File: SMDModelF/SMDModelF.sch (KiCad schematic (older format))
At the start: 45 parts, among them J1 Model F Ribbon Cable, J2 PadsToShort, J3 EXPANSION HEADER, J4 3178 Ribbon Cable, J6 MODEL F AT LOCKLIGHTS HEADER, U1 MCP4921-E, U2 LM339A, U3 74AHC595, U4 74AHC595, U5 ProMicro, U6 LM339A

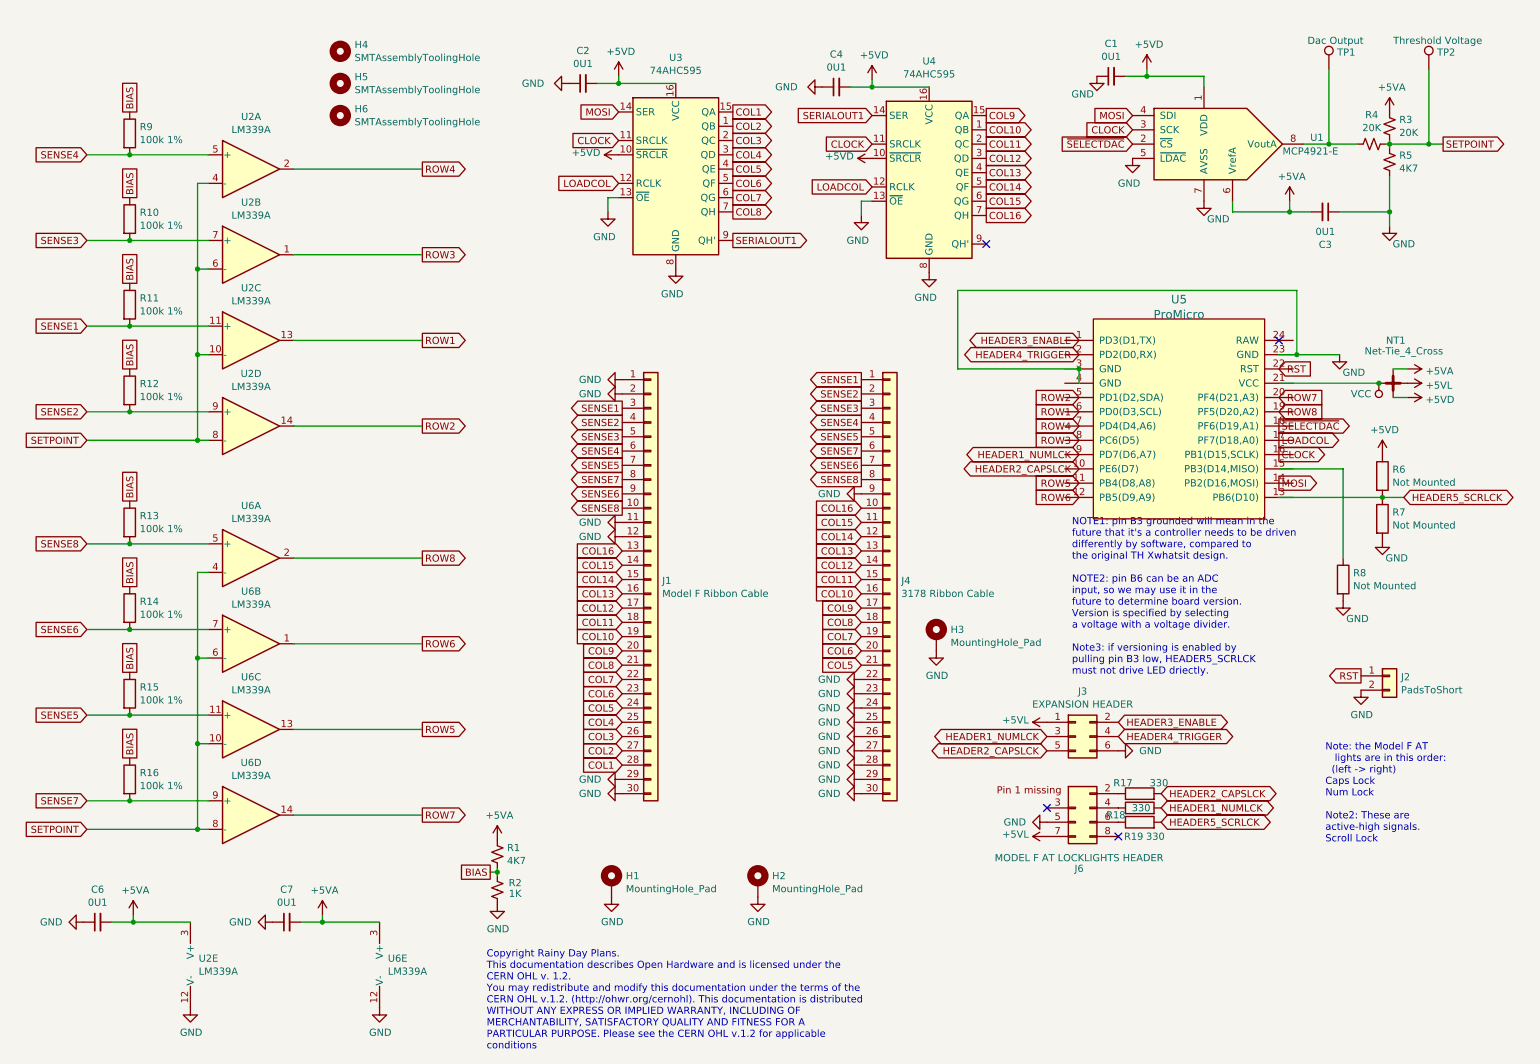
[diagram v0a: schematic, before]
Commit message: Added extra columns
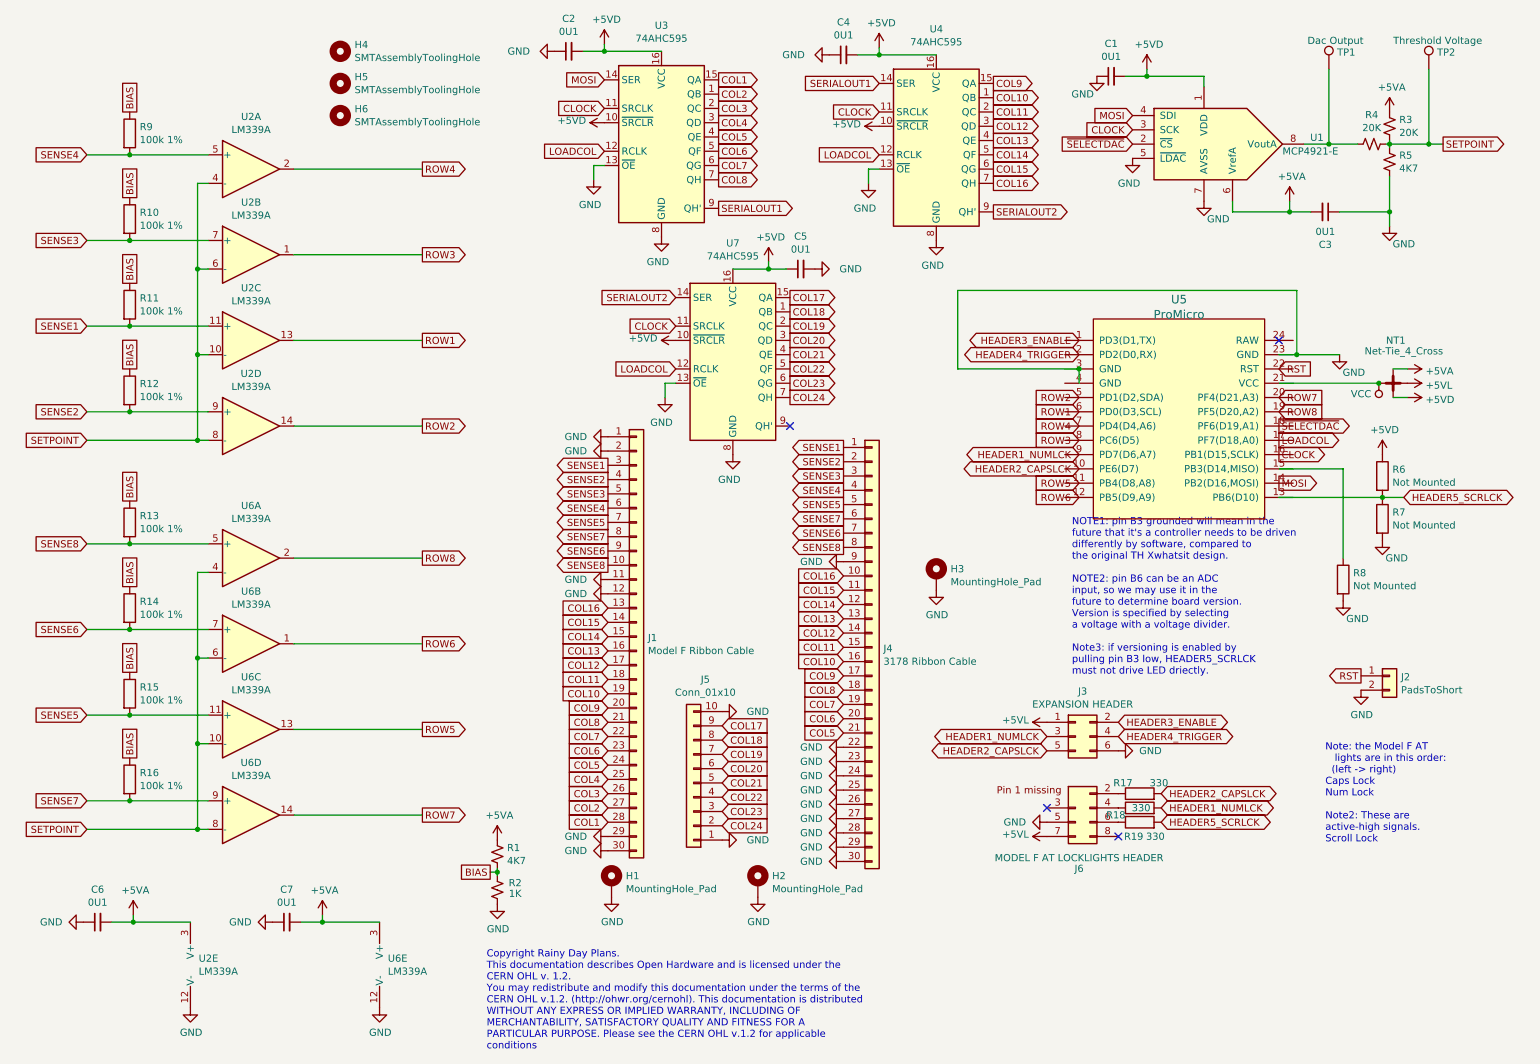
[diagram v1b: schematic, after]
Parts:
- added C5: 0U1, Capacitor_SMD:C_0805_2012Metric_Pad1.15x1.40mm_HandSolder, symbol Device:C_Small
- added J5: Conn_01x10, Connector_PinHeader_2.54mm:PinHeader_1x10_P2.54mm_Vertical, symbol Connector_Generic:Conn_01x10
- added U7: 74AHC595, Package_SO:SOIC-16_3.9x9.9mm_P1.27mm, symbol 74xx:74HCT595
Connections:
- net labels added: COL17, COL18, COL19, COL20, COL21, COL22, COL23, COL24, SERIALOUT2
- wire segments 93 -> 98
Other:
- moved on the sheet: C2, C4, H3, J1, J4, U3, U4

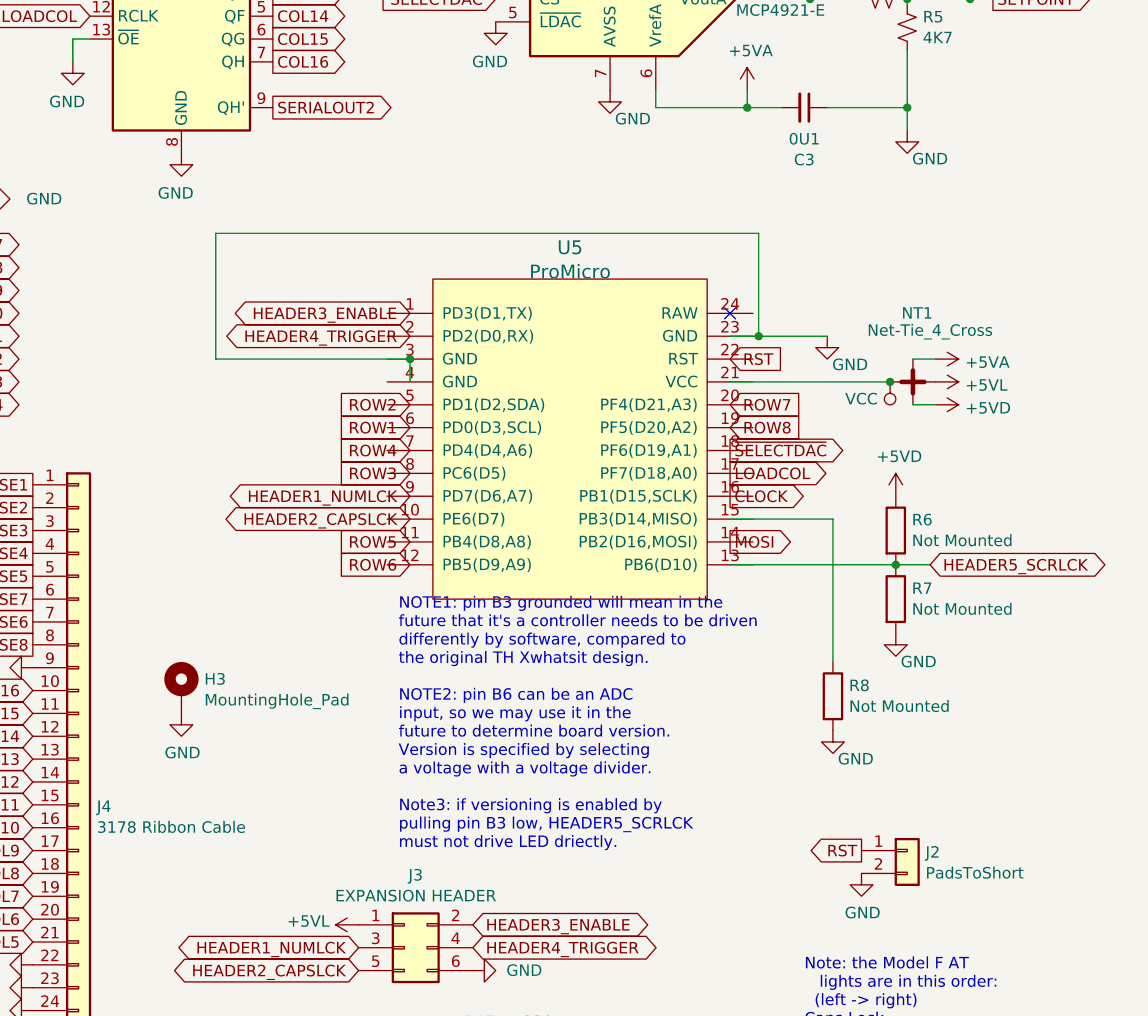
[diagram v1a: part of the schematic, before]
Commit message: Updated pro micro schematic symbol, and added PDF schematics
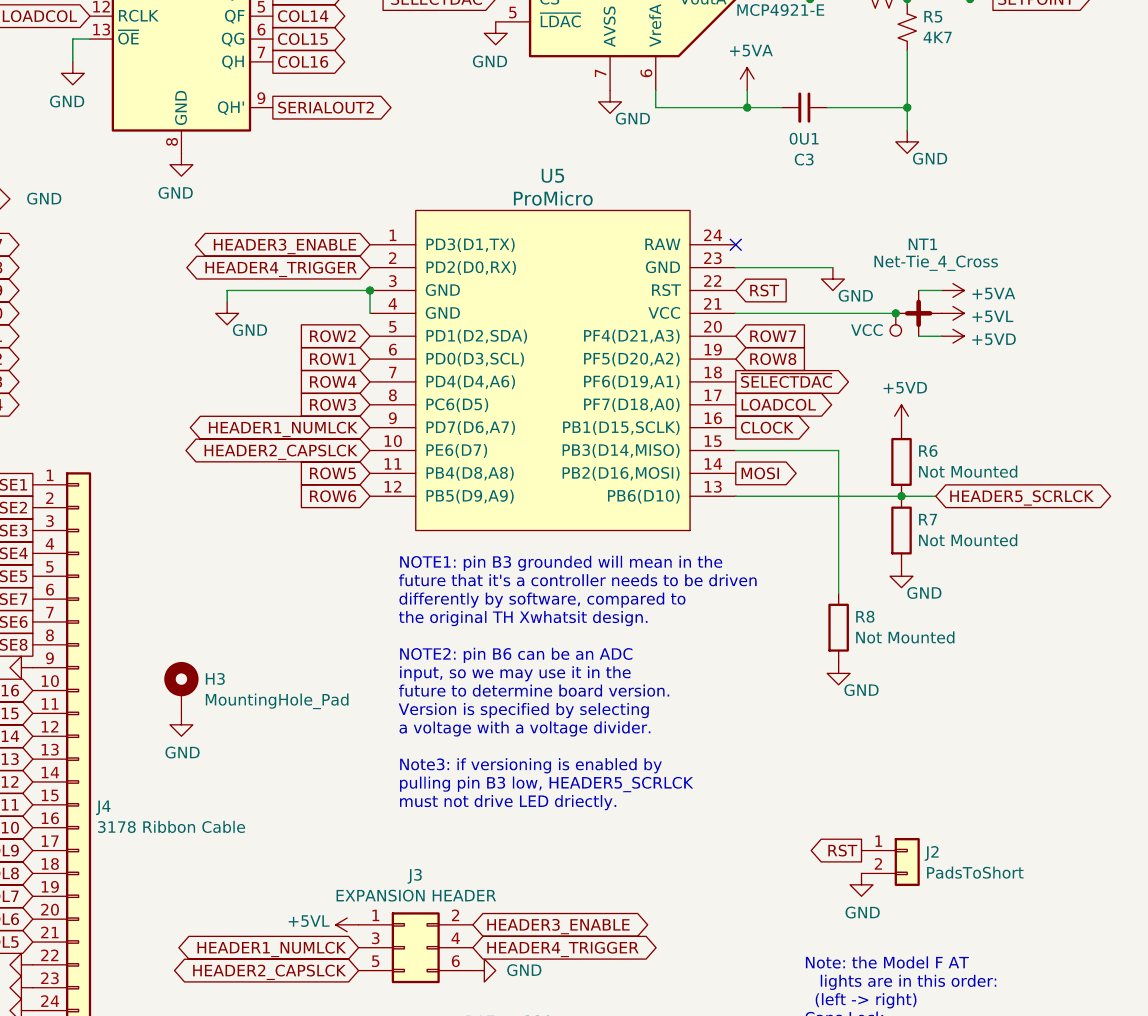
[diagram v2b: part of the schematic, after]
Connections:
- wire segments 98 -> 95
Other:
- moved on the sheet: NT1, R6, R7, R8, U5

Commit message: Ported over some changes from the 'standard' model F controller, to make 3d rendering look better
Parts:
- J3: footprint Connector_PinHeader_2.54mm:PinHeader_2x03_P2.54mm_Vertical -> TH-XWhatsIt:PinHeader_2x03_P2.54mm_Vertical_3dhorizontal
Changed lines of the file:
@@
 F 0 "J3" H 8125 5867 50  0000 C CNN
 F 1 "EXPANSION HEADER" H 8125 5776 50  0000 C CNN
-F 2 "Connector_PinHeader_2.54mm:PinHeader_2x03_P2.54mm_Vertical" H 8075 5550 50  0001 C CNN
+F 2 "TH-XWhatsIt:PinHeader_2x03_P2.54mm_Vertical_3dhorizontal" H 8075 5550 50  0001 C CNN
 F 3 "~" H 8075 5550 50  0001 C CNN
 	1    8075 5550

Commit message: Updated 100k resistor and shift register LCSC part numbers
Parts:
- R10, R11, R12, R13, R14, R15, R16, R9: LCSC C17407 -> C149504
- U3, U4, U7: LCSC C5520 -> C2682116
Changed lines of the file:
@@
 F 2 "Package_SO:SOIC-16_3.9x9.9mm_P1.27mm" H 5175 1350 50  0001 C CNN
 F 3 "https://assets.nexperia.com/documents/data-sheet/74HC_HCT595.pdf" H 5175 1350 50  0001 C CNN
-F 4 "C5520" H 5175 1350 50  0001 C CNN "LCSC"
+F 4 "C2682116" H 5175 1350 50  0001 C CNN "LCSC"
 	1    5175 1350
 	1    0    0    -1
@@
 F 2 "Resistor_SMD:R_0805_2012Metric_Pad1.15x1.40mm_HandSolder" V 1380 1325 50  0001 C CNN
 F 3 "~" H 1450 1325 50  0001 C CNN
-F 4 "C17407" H 1450 1325 50  0001 C CNN "LCSC"
+F 4 "C149504" H 1450 1325 50  0001 C CNN "LCSC"
 	1    1450 1325
 	1    0    0    -1
@@
 F 2 "Resistor_SMD:R_0805_2012Metric_Pad1.15x1.40mm_HandSolder" V 1380 1925 50  0001 C CNN
 F 3 "~" H 1450 1925 50  0001 C CNN
-F 4 "C17407" H 1450 1925 50  0001 C CNN "LCSC"
+F 4 "C149504" H 1450 1925 50  0001 C CNN "LCSC"
 	1    1450 1925
 	1    0    0    -1
@@
 F 2 "Resistor_SMD:R_0805_2012Metric_Pad1.15x1.40mm_HandSolder" V 1380 2525 50  0001 C CNN
 F 3 "~" H 1450 2525 50  0001 C CNN
-F 4 "C17407" H 1450 2525 50  0001 C CNN "LCSC"
+F 4 "C149504" H 1450 2525 50  0001 C CNN "LCSC"
 	1    1450 2525
 	1    0    0    -1
@@
 F 2 "Resistor_SMD:R_0805_2012Metric_Pad1.15x1.40mm_HandSolder" V 1380 3125 50  0001 C CNN
 F 3 "~" H 1450 3125 50  0001 C CNN
-F 4 "C17407" H 1450 3125 50  0001 C CNN "LCSC"
+F 4 "C149504" H 1450 3125 50  0001 C CNN "LCSC"
 	1    1450 3125
 	1    0    0    -1
@@
 F 2 "Resistor_SMD:R_0805_2012Metric_Pad1.15x1.40mm_HandSolder" V 1380 4050 50  0001 C CNN
 F 3 "~" H 1450 4050 50  0001 C CNN
-F 4 "C17407" H 1450 4050 50  0001 C CNN "LCSC"
+F 4 "C149504" H 1450 4050 50  0001 C CNN "LCSC"
 	1    1450 4050
 	1    0    0    -1
@@
 F 2 "Resistor_SMD:R_0805_2012Metric_Pad1.15x1.40mm_HandSolder" V 1380 4650 50  0001 C CNN
 F 3 "~" H 1450 4650 50  0001 C CNN
-F 4 "C17407" H 1450 4650 50  0001 C CNN "LCSC"
+F 4 "C149504" H 1450 4650 50  0001 C CNN "LCSC"
 	1    1450 4650
 	1    0    0    -1
@@
 F 2 "Resistor_SMD:R_0805_2012Metric_Pad1.15x1.40mm_HandSolder" V 1380 5250 50  0001 C CNN
 F 3 "~" H 1450 5250 50  0001 C CNN
-F 4 "C17407" H 1450 5250 50  0001 C CNN "LCSC"
+F 4 "C149504" H 1450 5250 50  0001 C CNN "LCSC"
 	1    1450 5250
 	1    0    0    -1
@@
 F 2 "Resistor_SMD:R_0805_2012Metric_Pad1.15x1.40mm_HandSolder" V 1380 5850 50  0001 C CNN
 F 3 "~" H 1450 5850 50  0001 C CNN
-F 4 "C17407" H 1450 5850 50  0001 C CNN "LCSC"
+F 4 "C149504" H 1450 5850 50  0001 C CNN "LCSC"
 	1    1450 5850
 	1    0    0    -1
@@
 F 2 "Package_SO:SOIC-16_3.9x9.9mm_P1.27mm" H 5675 2875 50  0001 C CNN
 F 3 "https://assets.nexperia.com/documents/data-sheet/74HC_HCT595.pdf" H 5675 2875 50  0001 C CNN
-F 4 "C5520" H 5675 2875 50  0001 C CNN "LCSC"
+F 4 "C2682116" H 5675 2875 50  0001 C CNN "LCSC"
 	1    5675 2875
 	1    0    0    -1
@@
 F 2 "Package_SO:SOIC-16_3.9x9.9mm_P1.27mm" H 7100 1375 50  0001 C CNN
 F 3 "https://assets.nexperia.com/documents/data-sheet/74HC_HCT595.pdf" H 7100 1375 50  0001 C CNN
-F 4 "C5520" H 7100 1375 50  0001 C CNN "LCSC"
+F 4 "C2682116" H 7100 1375 50  0001 C CNN "LCSC"
 	1    7100 1375
 	1    0    0    -1

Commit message: Revert part of commit 'Updated 100k resistor and shift register LCSC part numbers' (the shift register BOM changes only)
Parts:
- U3, U4, U7: LCSC C2682116 -> C5520
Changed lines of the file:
@@
 F 2 "Package_SO:SOIC-16_3.9x9.9mm_P1.27mm" H 5175 1350 50  0001 C CNN
 F 3 "https://assets.nexperia.com/documents/data-sheet/74HC_HCT595.pdf" H 5175 1350 50  0001 C CNN
-F 4 "C2682116" H 5175 1350 50  0001 C CNN "LCSC"
+F 4 "C5520" H 5175 1350 50  0001 C CNN "LCSC"
 	1    5175 1350
 	1    0    0    -1
@@
 F 2 "Package_SO:SOIC-16_3.9x9.9mm_P1.27mm" H 5675 2875 50  0001 C CNN
 F 3 "https://assets.nexperia.com/documents/data-sheet/74HC_HCT595.pdf" H 5675 2875 50  0001 C CNN
-F 4 "C2682116" H 5675 2875 50  0001 C CNN "LCSC"
+F 4 "C5520" H 5675 2875 50  0001 C CNN "LCSC"
 	1    5675 2875
 	1    0    0    -1
@@
 F 2 "Package_SO:SOIC-16_3.9x9.9mm_P1.27mm" H 7100 1375 50  0001 C CNN
 F 3 "https://assets.nexperia.com/documents/data-sheet/74HC_HCT595.pdf" H 7100 1375 50  0001 C CNN
-F 4 "C2682116" H 7100 1375 50  0001 C CNN "LCSC"
+F 4 "C5520" H 7100 1375 50  0001 C CNN "LCSC"
 	1    7100 1375
 	1    0    0    -1
